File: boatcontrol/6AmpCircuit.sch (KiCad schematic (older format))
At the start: 5 parts, among them K8701 G5RL-K1A-E-DC12, Q8701 T9-818 6A, SW8701 ESB30, SW8702 ESB30

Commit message: Fix graphics
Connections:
- net OFF_COIL: now reaches K8701.8 (C8), SW8702.2 (B), SW8702.5 (B)
- net TO_FUSE: now reaches K8701.4 (NO), K8701.5 (NO), Q8701.P1 (P?)
- net ON_COIL: now reaches K8701.1 (C1), SW8701.2 (B), SW8701.5 (B)
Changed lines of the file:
@@
 $Descr A4 11693 8268
 encoding utf-8
-Sheet 85 87
+Sheet 60 87
 Title "Boat Control Hat"
 Date "2020-07-09"
@@
 Wire Wire Line
 	6650 4000 6400 4000
+Text Label 6750 3550 0    50   ~ 0
+ON_COIL
+Text Label 6700 4500 0    50   ~ 0
+OFF_COIL
+Text Label 7350 3650 0    50   ~ 0
+TO_FUSE
 $EndSCHEMATC

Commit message: Make 12V PSU Optional
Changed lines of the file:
@@
 $Descr A4 11693 8268
 encoding utf-8
-Sheet 60 87
+Sheet 86 87
 Title "Boat Control Hat"
 Date "2020-07-09"
@@
 AR Path="/D1BB8DB4/5F746103/60365C49/D2F4D9A7" Ref="D5901"  Part="1"
 AR Path="/D1BB8DB4/5F746103/60365C53/D2F4D9A7" Ref="D6001"  Part="1"
-F 0 "D8701" H 5900 3850 50  0000 C CNN
+F 0 "D8601" H 5900 3850 50  0000 C CNN
 F 1 "20mA R/G" H 6050 3750 50  0000 C CNN
 F 2 "LED_THT:LED_D5.0mm-3" H 6100 4000 50  0001 C CNN
@@
 AR Path="/D1BB8DB4/5F746103/60365C49/D2F4DB56" Ref="K5901"  Part="1"
 AR Path="/D1BB8DB4/5F746103/60365C53/D2F4DB56" Ref="K6001"  Part="1"
-F 0 "K8701" H 7250 4000 50  0000 L CNN
+F 0 "K8601" H 7250 4000 50  0000 L CNN
 F 1 "G5RL-K1A-E-DC12" H 7600 4000 50  0000 L CNN
 F 2 "RELAY_G5RL-K1A-E-DC12" H 7600 4150 50  0001 L BNN
@@
 AR Path="/D1BB8DB4/5F746103/60365C49/D2F4D9AA" Ref="Q5901"  Part="1"
 AR Path="/D1BB8DB4/5F746103/60365C53/D2F4D9AA" Ref="Q6001"  Part="1"
-F 0 "Q8701" V 7150 2950 50  0000 R CNN
+F 0 "Q8601" V 7150 2950 50  0000 R CNN
 F 1 "T9-818 6A" V 7150 2700 50  0000 R CNN
 F 2 "BoatControl:Schurter_Circuit_Breaker" H 7150 3300 50  0001 C CNN
@@
 AR Path="/D1BB8DB4/5F746103/60365C49/D2F4D9AB" Ref="SW5901"  Part="1"
 AR Path="/D1BB8DB4/5F746103/60365C53/D2F4D9AB" Ref="SW6001"  Part="1"
-F 0 "SW8701" V 6050 3900 50  0000 C CNN
+F 0 "SW8601" V 6050 3900 50  0000 C CNN
 F 1 " ESB30" V 6000 3400 50  0000 C CNN
 F 2 "BoatControl:SW_PUSH_ESB30_DPDT" H 6050 3550 50  0001 C CNN
@@
 AR Path="/D1BB8DB4/5F746103/60365C49/E14E202C" Ref="#PWR05902"  Part="1"
 AR Path="/D1BB8DB4/5F746103/60365C53/E14E202C" Ref="#PWR06002"  Part="1"
-F 0 "#PWR08702" H 6650 3850 50  0001 C CNN
+F 0 "#PWR08602" H 6650 3850 50  0001 C CNN
 F 1 "+12P" H 6665 4173 50  0000 C CNN
 F 2 "" H 6650 4000 50  0001 C CNN
@@
 AR Path="/D1BB8DB4/5F746103/60365C49/D2F4D9A9" Ref="SW5902"  Part="1"
 AR Path="/D1BB8DB4/5F746103/60365C53/D2F4D9A9" Ref="SW6002"  Part="1"
-F 0 "SW8702" V 6050 5250 50  0000 C CNN
+F 0 "SW8602" V 6050 5250 50  0000 C CNN
 F 1 " ESB30" V 6000 4700 50  0000 C CNN
 F 2 "BoatControl:SW_PUSH_ESB30_DPDT" H 6050 4900 50  0001 C CNN
@@
 AR Path="/D1BB8DB4/5F746103/60365C49/D2F4D9AC" Ref="#PWR05901"  Part="1"
 AR Path="/D1BB8DB4/5F746103/60365C53/D2F4D9AC" Ref="#PWR06001"  Part="1"
-F 0 "#PWR08701" H 5250 3750 50  0001 C CNN
+F 0 "#PWR08601" H 5250 3750 50  0001 C CNN
 F 1 "GND" V 5255 3827 50  0000 C CNN
 F 2 "" H 5250 4000 50  0001 C CNN

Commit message: Logo stuff
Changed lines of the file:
@@
 AR Path="/D1BB8DB4/5F746103/60365C49/D2F4D9A7" Ref="D5901"  Part="1"
 AR Path="/D1BB8DB4/5F746103/60365C53/D2F4D9A7" Ref="D6001"  Part="1"
-F 0 "D8601" H 5900 3850 50  0000 C CNN
+F 0 "D8701" H 5900 3850 50  0000 C CNN
 F 1 "20mA R/G" H 6050 3750 50  0000 C CNN
 F 2 "LED_THT:LED_D5.0mm-3" H 6100 4000 50  0001 C CNN
@@
 AR Path="/D1BB8DB4/5F746103/60365C49/D2F4DB56" Ref="K5901"  Part="1"
 AR Path="/D1BB8DB4/5F746103/60365C53/D2F4DB56" Ref="K6001"  Part="1"
-F 0 "K8601" H 7250 4000 50  0000 L CNN
+F 0 "K8701" H 7250 4000 50  0000 L CNN
 F 1 "G5RL-K1A-E-DC12" H 7600 4000 50  0000 L CNN
 F 2 "RELAY_G5RL-K1A-E-DC12" H 7600 4150 50  0001 L BNN
@@
 AR Path="/D1BB8DB4/5F746103/60365C49/D2F4D9AA" Ref="Q5901"  Part="1"
 AR Path="/D1BB8DB4/5F746103/60365C53/D2F4D9AA" Ref="Q6001"  Part="1"
-F 0 "Q8601" V 7150 2950 50  0000 R CNN
+F 0 "Q8701" V 7150 2950 50  0000 R CNN
 F 1 "T9-818 6A" V 7150 2700 50  0000 R CNN
 F 2 "BoatControl:Schurter_Circuit_Breaker" H 7150 3300 50  0001 C CNN
@@
 AR Path="/D1BB8DB4/5F746103/60365C49/D2F4D9AB" Ref="SW5901"  Part="1"
 AR Path="/D1BB8DB4/5F746103/60365C53/D2F4D9AB" Ref="SW6001"  Part="1"
-F 0 "SW8601" V 6050 3900 50  0000 C CNN
+F 0 "SW8701" V 6050 3900 50  0000 C CNN
 F 1 " ESB30" V 6000 3400 50  0000 C CNN
 F 2 "BoatControl:SW_PUSH_ESB30_DPDT" H 6050 3550 50  0001 C CNN
@@
 AR Path="/D1BB8DB4/5F746103/60365C49/E14E202C" Ref="#PWR05902"  Part="1"
 AR Path="/D1BB8DB4/5F746103/60365C53/E14E202C" Ref="#PWR06002"  Part="1"
-F 0 "#PWR08602" H 6650 3850 50  0001 C CNN
+F 0 "#PWR08702" H 6650 3850 50  0001 C CNN
 F 1 "+12P" H 6665 4173 50  0000 C CNN
 F 2 "" H 6650 4000 50  0001 C CNN
@@
 AR Path="/D1BB8DB4/5F746103/60365C49/D2F4D9A9" Ref="SW5902"  Part="1"
 AR Path="/D1BB8DB4/5F746103/60365C53/D2F4D9A9" Ref="SW6002"  Part="1"
-F 0 "SW8602" V 6050 5250 50  0000 C CNN
+F 0 "SW8702" V 6050 5250 50  0000 C CNN
 F 1 " ESB30" V 6000 4700 50  0000 C CNN
 F 2 "BoatControl:SW_PUSH_ESB30_DPDT" H 6050 4900 50  0001 C CNN
@@
 AR Path="/D1BB8DB4/5F746103/60365C49/D2F4D9AC" Ref="#PWR05901"  Part="1"
 AR Path="/D1BB8DB4/5F746103/60365C53/D2F4D9AC" Ref="#PWR06001"  Part="1"
-F 0 "#PWR08601" H 5250 3750 50  0001 C CNN
+F 0 "#PWR08701" H 5250 3750 50  0001 C CNN
 F 1 "GND" V 5255 3827 50  0000 C CNN
 F 2 "" H 5250 4000 50  0001 C CNN

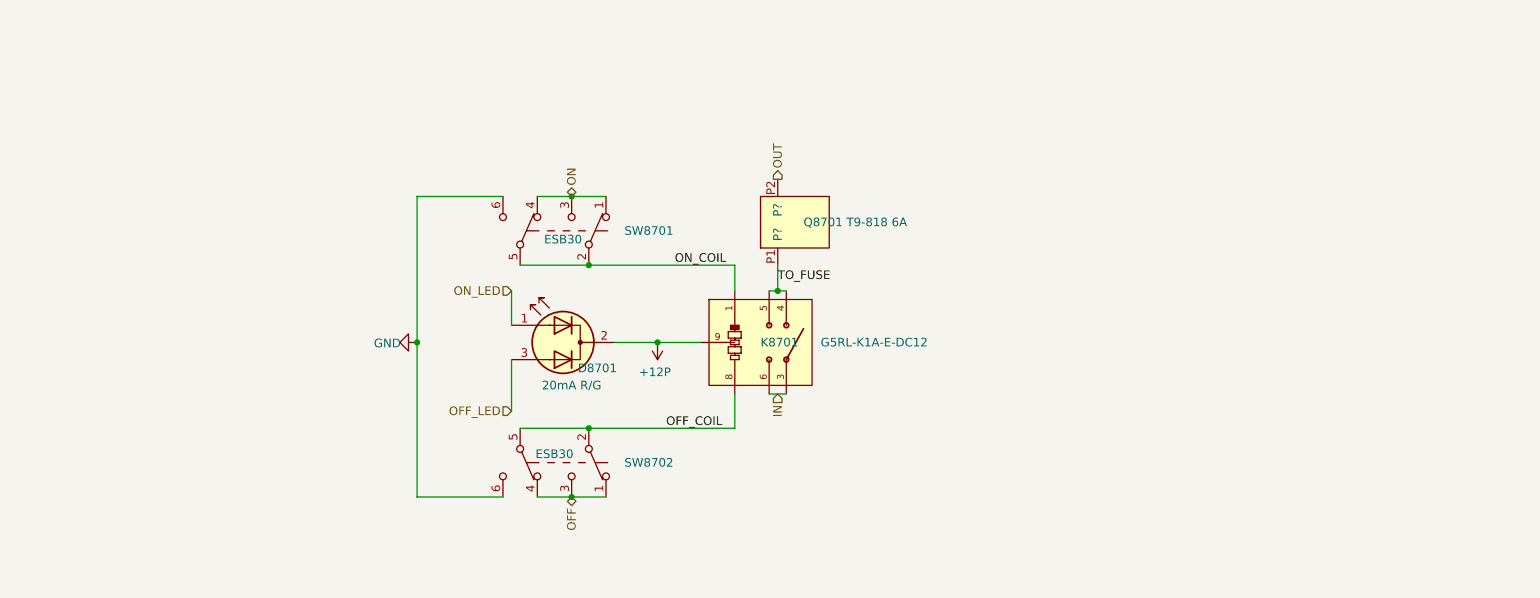
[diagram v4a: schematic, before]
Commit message: Fix switch layouts
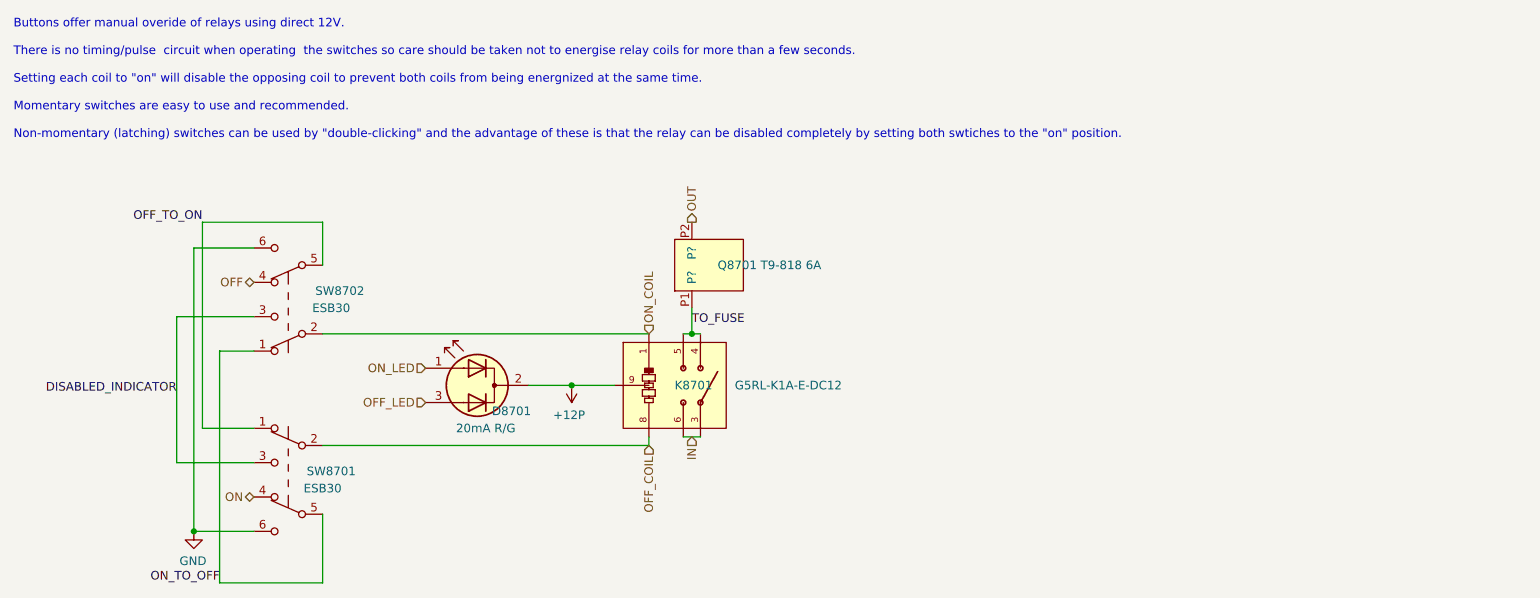
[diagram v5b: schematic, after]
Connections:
- net OFF: now also SW8701.4 (A); no longer SW8702.1 (A), SW8702.3 (C), SW8702.4 (A)
- net OFF_COIL: no longer SW8702.5 (B)
- net ON: now also SW8702.4 (A); no longer SW8701.1 (A), SW8701.3 (C), SW8701.4 (A)
- net ON_COIL: no longer SW8701.5 (B)
- new net DISABLED_INDICATOR: SW8701.3 (C), SW8702.3 (C)
- new net OFF_TO_ON: SW8701.5 (B), SW8702.1 (A)
- new net ON_TO_OFF: SW8701.1 (A), SW8702.5 (B)
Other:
- note added: "Buttons offer manual overide of relays using direct 12V.\n\nThere is no timing/pulse circuit when operating the switches so care should be taken not to energise relay coils for more than a few seconds.\n\nSetting each coil to "on" will disable the opposing coil to prevent both coils from being energnized at the same time.\n\nMomentary switches are easy to use and recommended.\n\nNon-momentary (la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"
- moved on the sheet: D8701, K8701, Q8701, SW8701, SW8702

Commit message: Move In
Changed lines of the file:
@@
 $Descr A4 11693 8268
 encoding utf-8
-Sheet 87 87
+Sheet 59 87
 Title "Boat Control Hat"
 Date "2020-07-09"
@@
 AR Path="/D1BB8DB4/5F746103/60365C49/D2F4D9A7" Ref="D5901"  Part="1"
 AR Path="/D1BB8DB4/5F746103/60365C53/D2F4D9A7" Ref="D6001"  Part="1"
-F 0 "D8701" H 5400 4100 50  0000 C CNN
+F 0 "D5701" H 5400 4100 50  0000 C CNN
 F 1 "20mA R/G" H 5550 4000 50  0000 C CNN
 F 2 "LED_THT:LED_D5.0mm-3" H 5600 4250 50  0001 C CNN
@@
 AR Path="/D1BB8DB4/5F746103/60365C49/D2F4DB56" Ref="K5901"  Part="1"
 AR Path="/D1BB8DB4/5F746103/60365C53/D2F4DB56" Ref="K6001"  Part="1"
-F 0 "K8701" H 6750 4250 50  0000 L CNN
+F 0 "K5701" H 6750 4250 50  0000 L CNN
 F 1 "G5RL-K1A-E-DC12" H 7100 4250 50  0000 L CNN
 F 2 "RELAY_G5RL-K1A-E-DC12" H 7100 4400 50  0001 L BNN
@@
 AR Path="/D1BB8DB4/5F746103/60365C49/D2F4D9AA" Ref="Q5901"  Part="1"
 AR Path="/D1BB8DB4/5F746103/60365C53/D2F4D9AA" Ref="Q6001"  Part="1"
-F 0 "Q8701" V 6650 3200 50  0000 R CNN
+F 0 "Q5701" V 6650 3200 50  0000 R CNN
 F 1 "T9-818 6A" V 6650 2950 50  0000 R CNN
 F 2 "BoatControl:Schurter_Circuit_Breaker" H 6650 3550 50  0001 C CNN
@@
 AR Path="/D1BB8DB4/5F746103/60365C49/D2F4D9AB" Ref="SW5901"  Part="1"
 AR Path="/D1BB8DB4/5F746103/60365C53/D2F4D9AB" Ref="SW6001"  Part="1"
-F 0 "SW8701" H 4250 4750 50  0000 C CNN
+F 0 "SW5701" H 4250 4750 50  0000 C CNN
 F 1 " ESB30" H 4250 3800 50  0000 C CNN
 F 2 "BoatControl:SW_PUSH_ESB30_DPDT" H 4500 3950 50  0001 C CNN
@@
 AR Path="/D1BB8DB4/5F746103/60365C49/D2F4D9A9" Ref="SW5902"  Part="1"
 AR Path="/D1BB8DB4/5F746103/60365C53/D2F4D9A9" Ref="SW6002"  Part="1"
-F 0 "SW8702" H 4200 5900 50  0000 C CNN
+F 0 "SW5702" H 4200 5900 50  0000 C CNN
 F 1 " ESB30" H 4300 4750 50  0000 C CNN
 F 2 "BoatControl:SW_PUSH_ESB30_DPDT" H 4500 5000 50  0001 C CNN
@@
 AR Path="/D1BB8DB4/5F75E923/60474907/60D74A5A" Ref="#PWR?"  Part="1"
 AR Path="/D1BB8DB4/5F75E923/60474911/60D74A5A" Ref="#PWR?"  Part="1"
-F 0 "#PWR0153" H 6150 4100 50  0001 C CNN
+F 0 "#PWR0151" H 6150 4100 50  0001 C CNN
 F 1 "+12P" H 6165 4423 50  0000 C CNN
 F 2 "" H 6150 4250 50  0001 C CNN
@@
 AR Path="/D1BB8DB4/5F75E923/60474907/60D74A7B" Ref="#PWR?"  Part="1"
 AR Path="/D1BB8DB4/5F75E923/60474911/60D74A7B" Ref="#PWR?"  Part="1"
-F 0 "#PWR0154" H 3950 4850 50  0001 C CNN
+F 0 "#PWR0152" H 3950 4850 50  0001 C CNN
 F 1 "GND" H 3955 4927 50  0000 C CNN
 F 2 "" H 3950 5100 50  0001 C CNN

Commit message: Figure out wiring cluster
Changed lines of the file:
@@
 $Descr A4 11693 8268
 encoding utf-8
-Sheet 59 87
+Sheet 85 87
 Title "Boat Control Hat"
 Date "2020-07-09"
@@
 AR Path="/D1BB8DB4/5F746103/60365C49/D2F4D9A7" Ref="D5901"  Part="1"
 AR Path="/D1BB8DB4/5F746103/60365C53/D2F4D9A7" Ref="D6001"  Part="1"
-F 0 "D5701" H 5400 4100 50  0000 C CNN
+F 0 "D8701" H 5400 4100 50  0000 C CNN
 F 1 "20mA R/G" H 5550 4000 50  0000 C CNN
 F 2 "LED_THT:LED_D5.0mm-3" H 5600 4250 50  0001 C CNN
@@
 AR Path="/D1BB8DB4/5F746103/60365C49/D2F4DB56" Ref="K5901"  Part="1"
 AR Path="/D1BB8DB4/5F746103/60365C53/D2F4DB56" Ref="K6001"  Part="1"
-F 0 "K5701" H 6750 4250 50  0000 L CNN
+F 0 "K8701" H 6750 4250 50  0000 L CNN
 F 1 "G5RL-K1A-E-DC12" H 7100 4250 50  0000 L CNN
 F 2 "RELAY_G5RL-K1A-E-DC12" H 7100 4400 50  0001 L BNN
@@
 AR Path="/D1BB8DB4/5F746103/60365C49/D2F4D9AA" Ref="Q5901"  Part="1"
 AR Path="/D1BB8DB4/5F746103/60365C53/D2F4D9AA" Ref="Q6001"  Part="1"
-F 0 "Q5701" V 6650 3200 50  0000 R CNN
+F 0 "Q8701" V 6650 3200 50  0000 R CNN
 F 1 "T9-818 6A" V 6650 2950 50  0000 R CNN
 F 2 "BoatControl:Schurter_Circuit_Breaker" H 6650 3550 50  0001 C CNN
@@
 AR Path="/D1BB8DB4/5F746103/60365C49/D2F4D9AB" Ref="SW5901"  Part="1"
 AR Path="/D1BB8DB4/5F746103/60365C53/D2F4D9AB" Ref="SW6001"  Part="1"
-F 0 "SW5701" H 4250 4750 50  0000 C CNN
+F 0 "SW8701" H 4250 4750 50  0000 C CNN
 F 1 " ESB30" H 4250 3800 50  0000 C CNN
 F 2 "BoatControl:SW_PUSH_ESB30_DPDT" H 4500 3950 50  0001 C CNN
@@
 AR Path="/D1BB8DB4/5F746103/60365C49/D2F4D9A9" Ref="SW5902"  Part="1"
 AR Path="/D1BB8DB4/5F746103/60365C53/D2F4D9A9" Ref="SW6002"  Part="1"
-F 0 "SW5702" H 4200 5900 50  0000 C CNN
+F 0 "SW8702" H 4200 5900 50  0000 C CNN
 F 1 " ESB30" H 4300 4750 50  0000 C CNN
 F 2 "BoatControl:SW_PUSH_ESB30_DPDT" H 4500 5000 50  0001 C CNN
